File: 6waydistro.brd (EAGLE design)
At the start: 100 x 50 mm, 36 parts, among them J1 POWERPOLE_POWER10AWG, J10 FUSEATC, J11 POWERPOLE_POWER10AWG, J12 FUSEATC, J2 FUSEATC, J3 POWERPOLE_POWER10AWG, J4 FUSEATC, J5 POWERPOLE_POWER10AWG, J6 FUSEATC, J7 POWERPOLE_POWER10AWG, J8 FUSEATC, J9 POWERPOLE_POWER10AWG

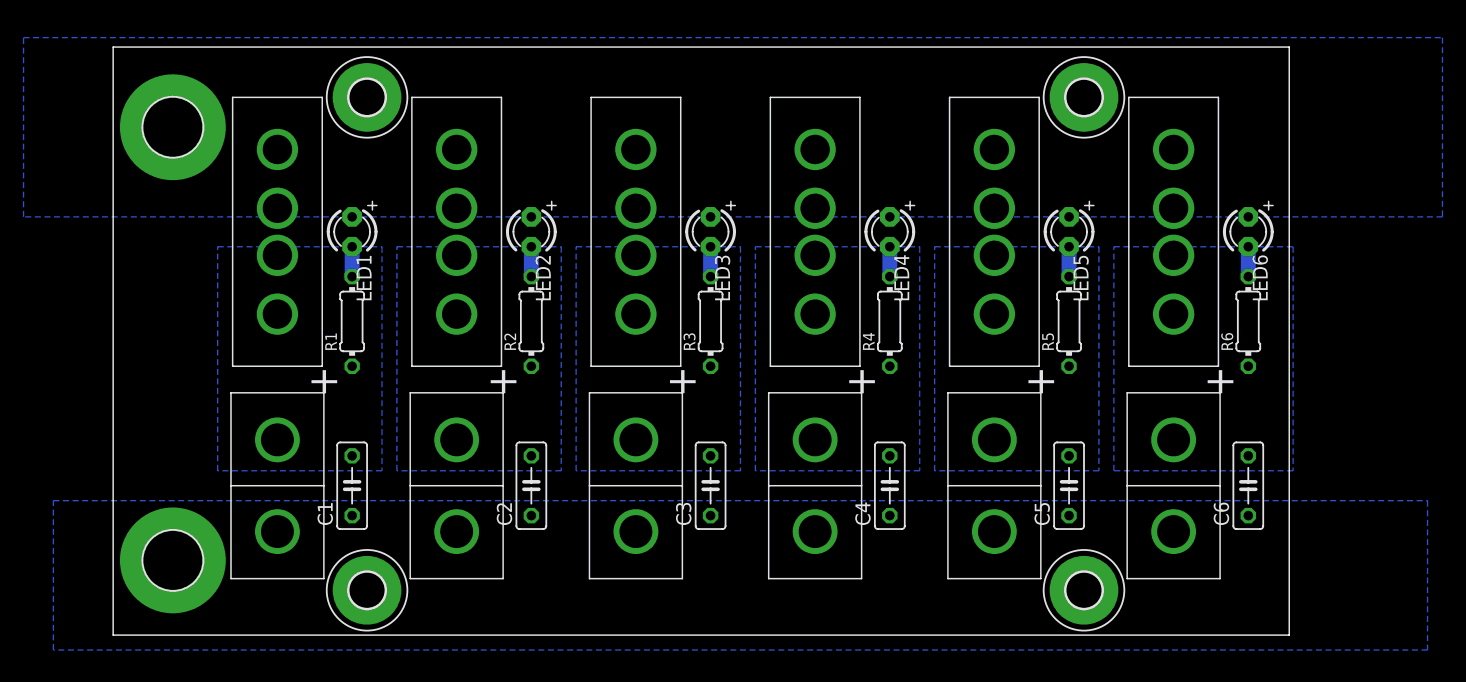
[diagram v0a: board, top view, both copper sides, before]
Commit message: Removed wire inlet holes and adjusted board layout for acrylic case
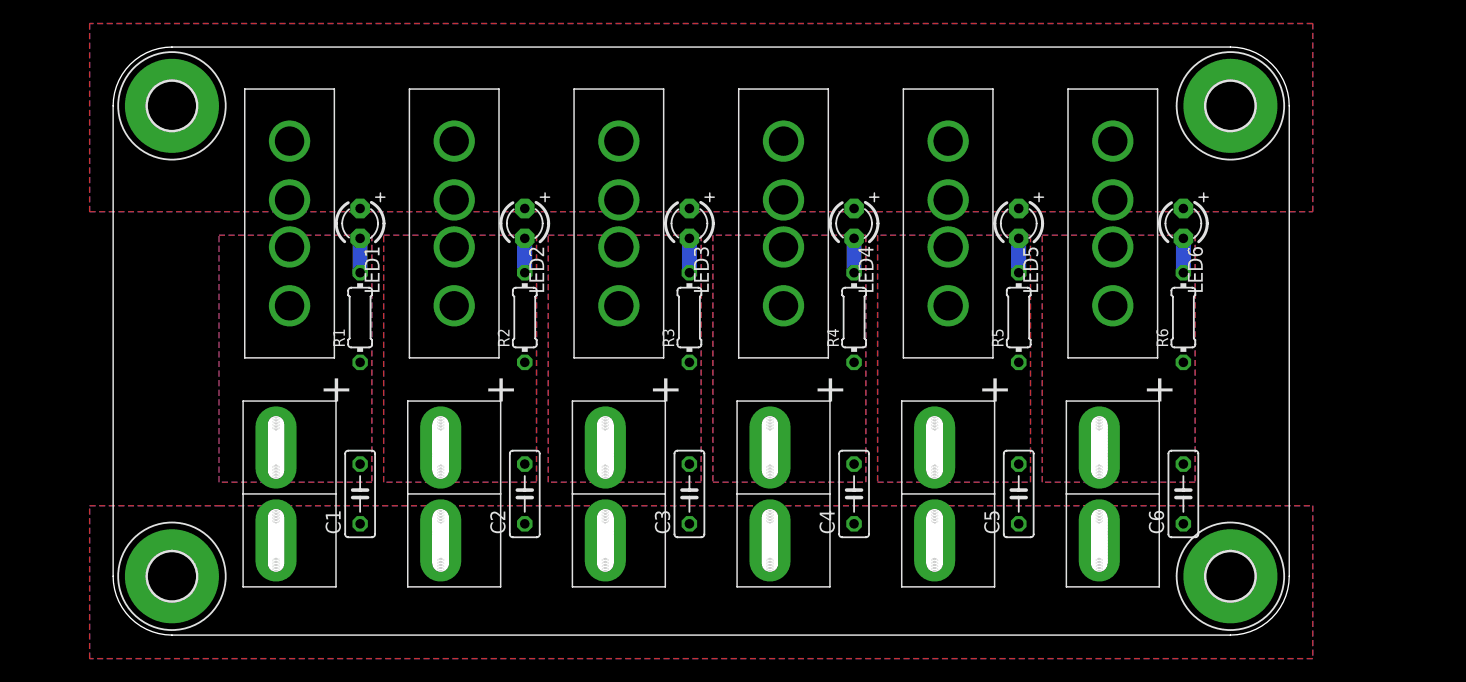
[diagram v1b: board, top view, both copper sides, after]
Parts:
- removed H1, H2: MOUNT-PAD-ROUND5.0, holes:5,0-PAD
- H3, H4, H5, H6: value MOUNT-PAD-ROUND3.0 -> MOUNT-PAD-ROUND4.1; device holes:3,0-PAD -> holes:4,1-PAD
- J1, J11, J3, J5, J7, J9: value POWERPOLE_POWER10AWG -> POWERPOLE_POWER45A; device powerpoles:POWERPOLE_PAIR_10AWG -> powerpoles:POWERPOLE_PAIR_45A
- moved H3 16.6 mm to (5.00, 5.00)
- moved H6 16.6 mm to (5.00, 45.0)
- moved H4 12.5 mm to (95.0, 5.00)
- moved H5 12.5 mm to (95.0, 45.0)
- moved LED6 5.57 mm to (91.0, 35.0)
- moved C6 5.56 mm to (91.0, 12.0)
- moved R6 5.53 mm to (91.0, 27.0)
- moved J12 5.22 mm to (85.0, 35.0)
- moved J11 5.22 mm to (85.0, 12.0)
- moved LED5 4.34 mm to (77.0, 35.0)
- moved C5 4.34 mm to (77.0, 12.0)
- moved R5 4.29 mm to (77.0, 27.0)
- moved J10 3.99 mm to (71.0, 35.0)
- moved J9 3.99 mm to (71.0, 12.0)
- moved LED4 3.12 mm to (63.0, 35.0)
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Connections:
- net GND: now also H3.B4,1, H4.B4,1; no longer H1.B5, H3.B3,0, H4.B3,0
- net VCC: no longer H2.B5
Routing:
- added copper zone on layer 1, net GND
- added copper zone on layer 1, net PPV1
- added copper zone on layer 1, net PPV2
- added copper zone on layer 1, net PPV3
- added copper zone on layer 1, net PPV4
- added copper zone on layer 1, net PPV5
- added copper zone on layer 1, net PPV6
- added copper zone on layer 1, net VCC
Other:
- outline, holes or cut-outs redrawn
